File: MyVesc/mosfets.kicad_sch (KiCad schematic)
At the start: 26 parts, among them J10 GATE_PH_A, J11 CURR_SENS_PH_A, J12 CURR_SENS_PH_B, J13 CURR_SENS_PH_C, J6 TEMP_SENS, J7 V_IN, J8 GATE_PH_C, J9 GATE_PH_B, U13 INA240, U14 INA240, U15 INA240, U16 MC74VHC1GT66, U17 MC74VHC1GT66, U18 MC74VHC1GT66

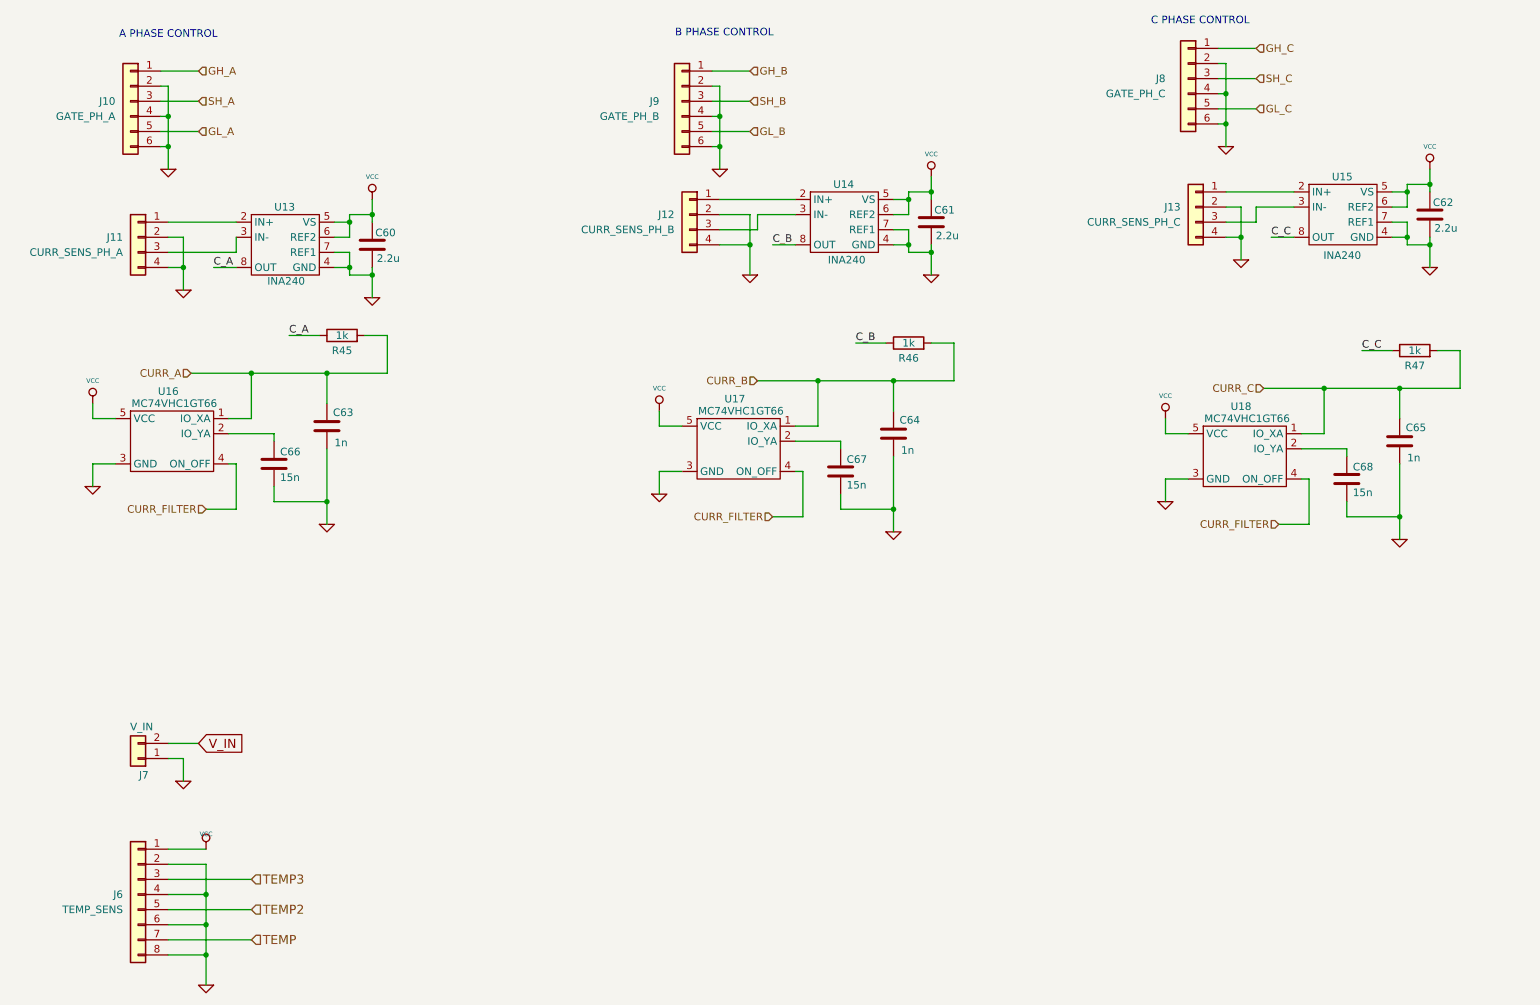
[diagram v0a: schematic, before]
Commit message: updated board for new mosfets
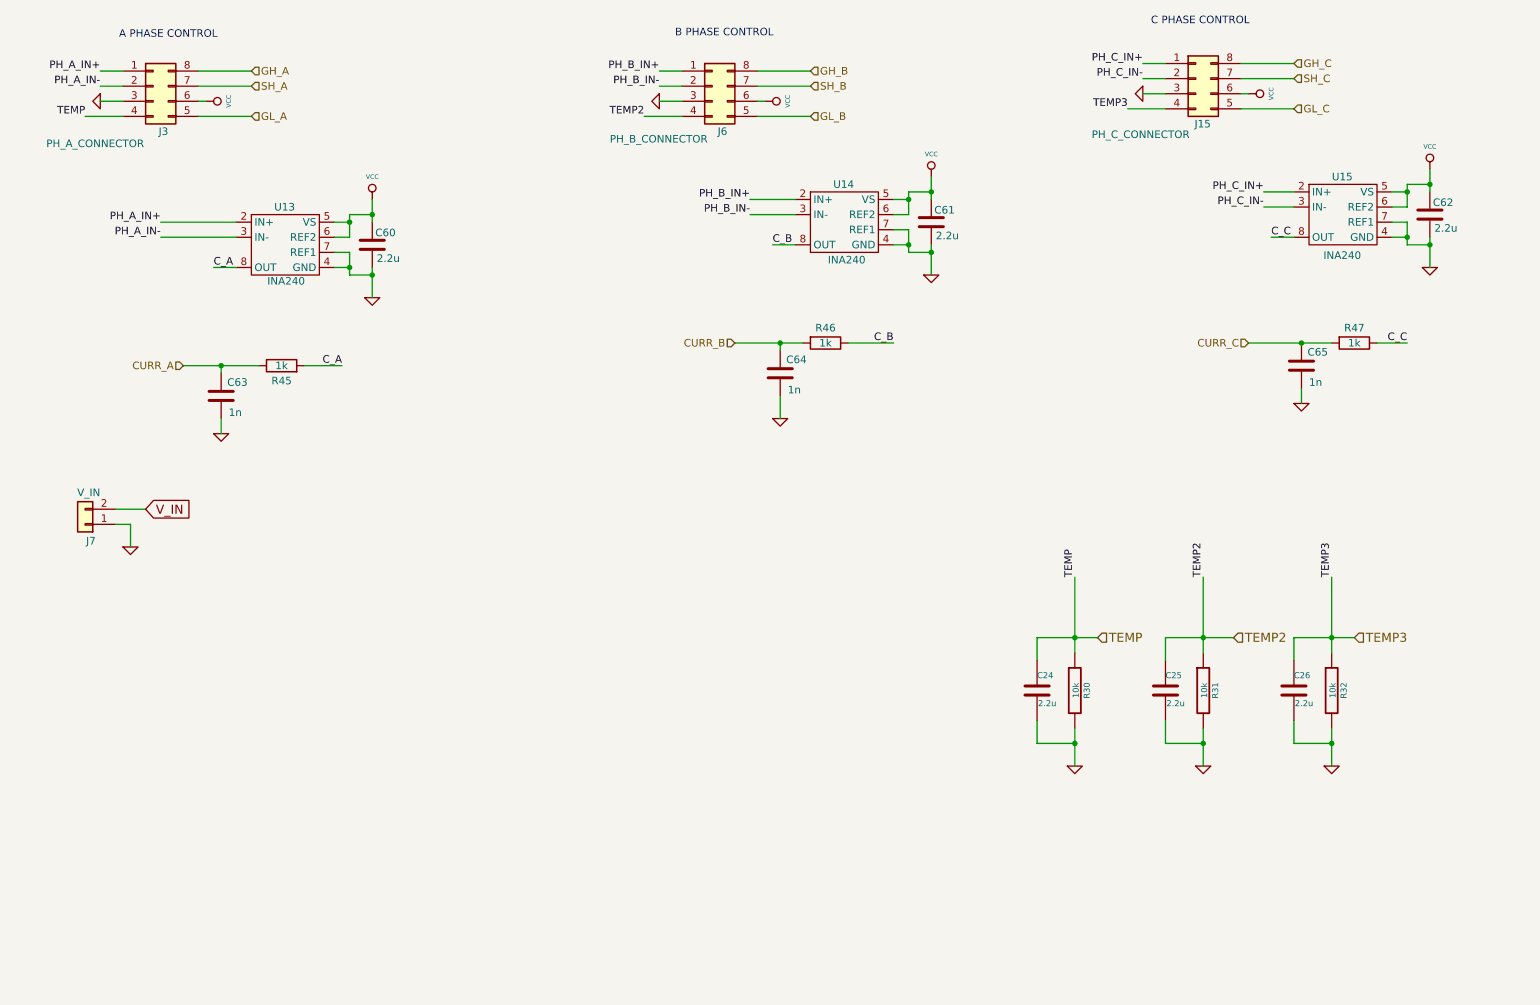
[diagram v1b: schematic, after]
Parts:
- removed C66, C67, C68: 15n, Capacitor_SMD:C_0603_1608Metric, symbol Device:C
- removed J10: GATE_PH_A, Connector_PinHeader_1.00mm:PinHeader_1x06_P1.00mm_Vertical, symbol Connector_Generic:Conn_01x06
- removed J11: CURR_SENS_PH_A, Connector_PinHeader_1.00mm:PinHeader_1x04_P1.00mm_Vertical, symbol Connector_Generic:Conn_01x04
- removed J12: CURR_SENS_PH_B, Connector_PinHeader_1.00mm:PinHeader_1x04_P1.00mm_Vertical, symbol Connector_Generic:Conn_01x04
- removed J13: CURR_SENS_PH_C, Connector_PinHeader_1.00mm:PinHeader_1x04_P1.00mm_Vertical, symbol Connector_Generic:Conn_01x04
- removed J6: TEMP_SENS, Connector_PinHeader_1.00mm:PinHeader_1x08_P1.00mm_Vertical, symbol Connector_Generic:Conn_01x08
- removed J8: GATE_PH_C, Connector_PinHeader_1.00mm:PinHeader_1x06_P1.00mm_Vertical, symbol Connector_Generic:Conn_01x06
- removed J9: GATE_PH_B, Connector_PinHeader_1.00mm:PinHeader_1x06_P1.00mm_Vertical, symbol Connector_Generic:Conn_01x06
- removed U16, U17, U18: MC74VHC1GT66, Package_SO:TSOP-5_1.65x3.05mm_P0.95mm, symbol MC74VHC1GT66:MC74VHC1GT66
- added C24, C25, C26: 2.2u, Capacitor_SMD:C_0603_1608Metric, symbol BLDC_4-rescue:C-RESCUE-BLDC_4
- added J15: PH_C_CONNECTOR, Connector_PinHeader_2.54mm:PinHeader_2x04_P2.54mm_Vertical, symbol Connector_Generic:Conn_02x04_Counter_Clockwise
- added J3: PH_A_CONNECTOR, Connector_PinHeader_2.54mm:PinHeader_2x04_P2.54mm_Vertical, symbol Connector_Generic:Conn_02x04_Counter_Clockwise
- added J6: PH_B_CONNECTOR, Connector_PinHeader_2.54mm:PinHeader_2x04_P2.54mm_Vertical, symbol Connector_Generic:Conn_02x04_Counter_Clockwise
- added R30, R31, R32: 10k, Resistor_SMD:R_0603_1608Metric, symbol BLDC_4-rescue:R-RESCUE-BLDC_4
- J7: footprint Connector_PinHeader_1.00mm:PinHeader_1x02_P1.00mm_Vertical -> Connector_PinSocket_2.54mm:PinSocket_1x02_P2.54mm_Vertical
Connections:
- net CURR_A: now also R45.1; no longer R45.2
- net C_A: now also R45.2; no longer R45.1
- net GH_A: now also J3.8 (Pin_8)
- net GH_B: now also J6.8 (Pin_8)
- net GH_C: now also J15.8 (Pin_8)
- net GL_A: now also J3.5 (Pin_5)
- net GL_B: now also J6.5 (Pin_5)
- net GL_C: now also J15.5 (Pin_5)
- net GND: now also C24.2, C25.2, C26.2, J15.3 (Pin_3), J3.3 (Pin_3), J6.3 (Pin_3), R30.2, R31.2, R32.2
- net SH_A: now also J3.7 (Pin_7)
- net SH_B: now also J6.7 (Pin_7)
- net SH_C: now also J15.7 (Pin_7)
- net TEMP: now also C24.1, J3.4 (Pin_4), R30.1
- net TEMP2: now also C25.1, J6.4 (Pin_4), R31.1
- net TEMP3: now also C26.1, J15.4 (Pin_4), R32.1
- net VCC: now also J15.6 (Pin_6), J3.6 (Pin_6), J6.6 (Pin_6)
- net PH_B_IN+: now reaches U14.2 (IN+)
- net PH_B_IN+: now also J6.1 (Pin_1)
- net PH_B_IN-: now reaches U14.3 (IN-)
- net PH_B_IN-: now also J6.2 (Pin_2)
- net PH_C_IN+: now reaches U15.2 (IN+)
- net PH_C_IN+: now also J15.1 (Pin_1)
- net PH_C_IN-: now reaches U15.3 (IN-)
- net PH_C_IN-: now also J15.2 (Pin_2)
- net PH_A_IN+: now reaches U13.2 (IN+)
- net PH_A_IN+: now also J3.1 (Pin_1)
- net PH_A_IN-: now reaches U13.3 (IN-)
- net PH_A_IN-: now also J3.2 (Pin_2)
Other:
- moved on the sheet: C63, C64, C65, J7, R45, R46, R47

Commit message: routerd logic board
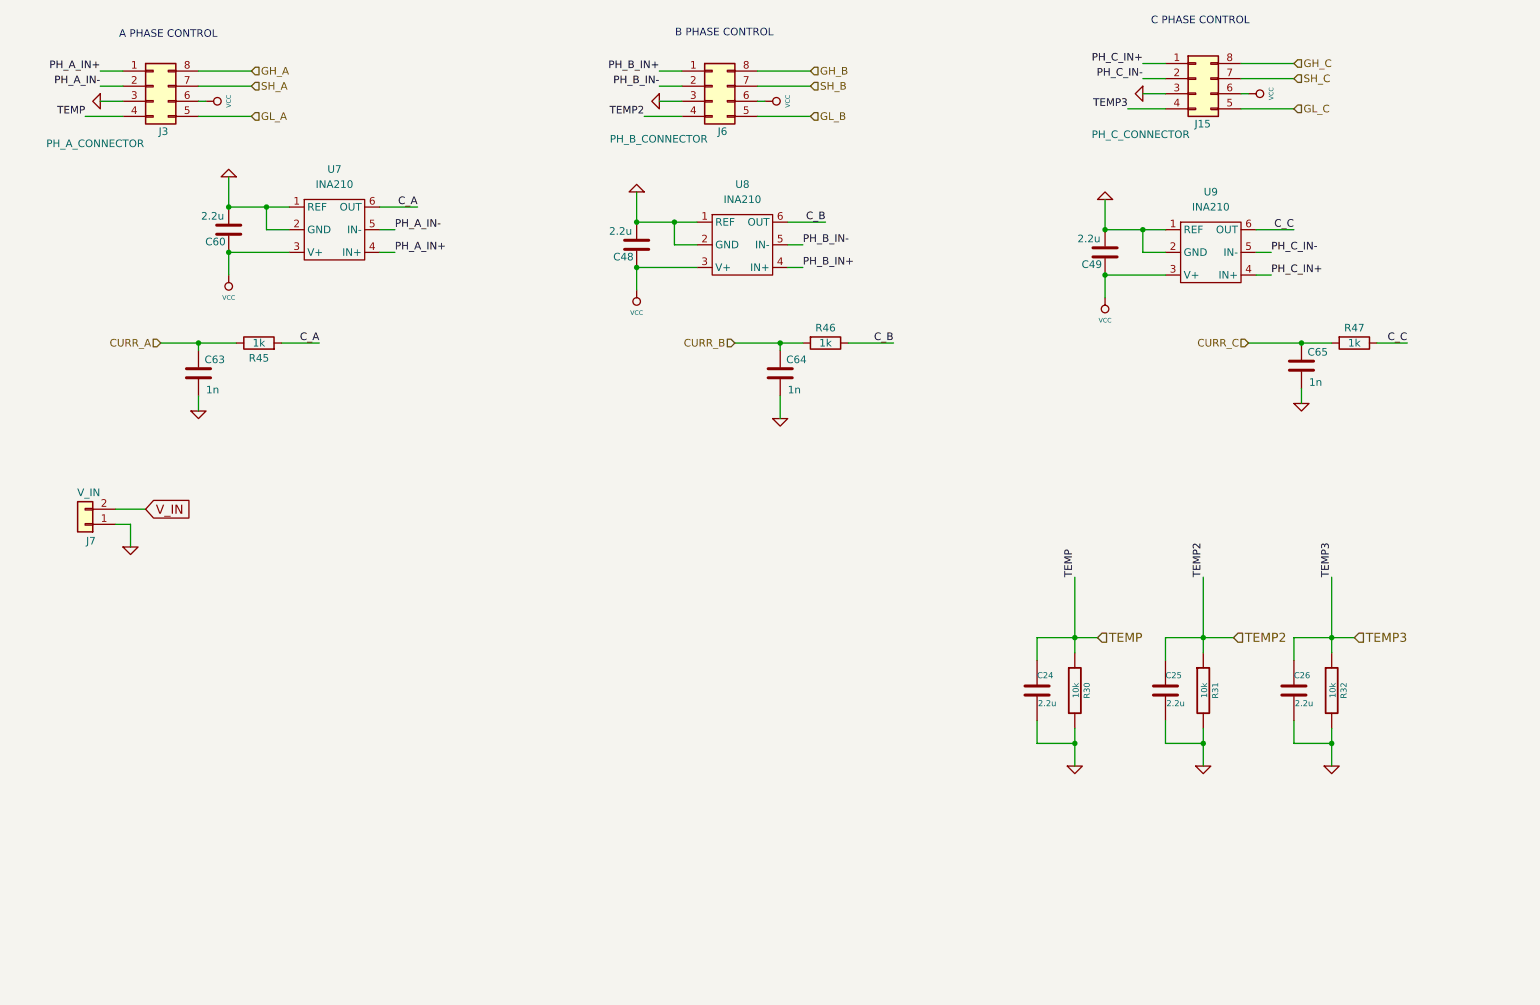
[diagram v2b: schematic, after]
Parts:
- removed C61, C62: 2.2u, Capacitor_SMD:C_0603_1608Metric, symbol Device:C
- removed U13, U14, U15: INA240, Package_SO:SOIC-8_3.9x4.9mm_P1.27mm, symbol INA240:INA240
- added C48, C49: 2.2u, Capacitor_SMD:C_0603_1608Metric, symbol Device:C
- added U7, U8, U9: INA210, Package_TO_SOT_SMD:SOT-363_SC-70-6, symbol INA240:INA210
- J15, J3, J6: footprint Connector_PinHeader_2.54mm:PinHeader_2x04_P2.54mm_Vertical -> Connector_PinSocket_2.54mm:PinSocket_2x04_P2.54mm_Vertical
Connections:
- net C_A: now also U7.6 (OUT)
- net C_B: now also U8.6 (OUT)
- net C_C: now also U9.6 (OUT)
- net GND: now also C48.2, C49.2, U7.1 (REF), U7.2 (GND), U8.1 (REF), U8.2 (GND), U9.1 (REF), U9.2 (GND)
- net PH_A_IN+: now also U7.4 (IN+)
- net PH_A_IN-: now also U7.5 (IN-)
- net PH_B_IN+: now also U8.4 (IN+)
- net PH_B_IN-: now also U8.5 (IN-)
- net PH_C_IN+: now also U9.4 (IN+)
- net PH_C_IN-: now also U9.5 (IN-)
- net VCC: now also C48.1, C49.1, U7.3 (V+), U8.3 (V+), U9.3 (V+)
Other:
- moved on the sheet: C60, C63, R45

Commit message: moved curr amps
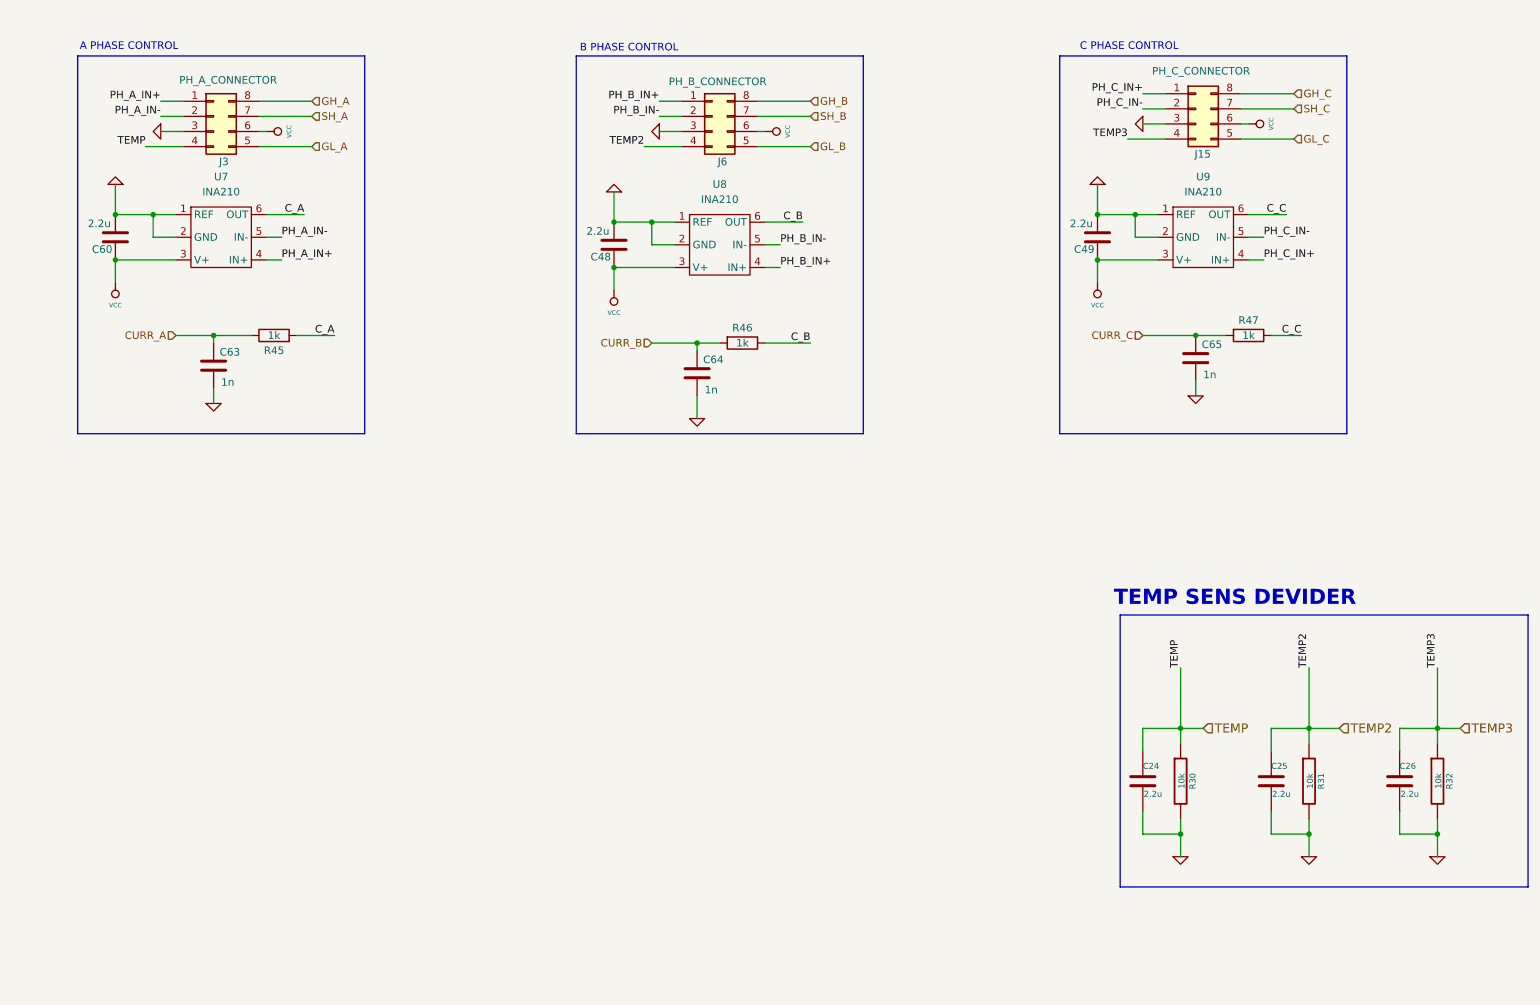
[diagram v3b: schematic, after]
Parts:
- removed J7: V_IN, Connector_PinSocket_2.54mm:PinSocket_1x02_P2.54mm_Vertical, symbol Connector_Generic:Conn_01x02
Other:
- note added: "TEMP SENS DEVIDER"
- moved on the sheet: C24, C25, C26, C48, C49, C60, C63, C64, C65, J15, J3, J6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
